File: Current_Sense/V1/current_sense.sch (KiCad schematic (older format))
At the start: 25 parts, among them J201 1935161, U201 LM4040CYM3-4.1-TR, U202 PGA281AIPWR, U203 ADC141S626CIMM/NOPB

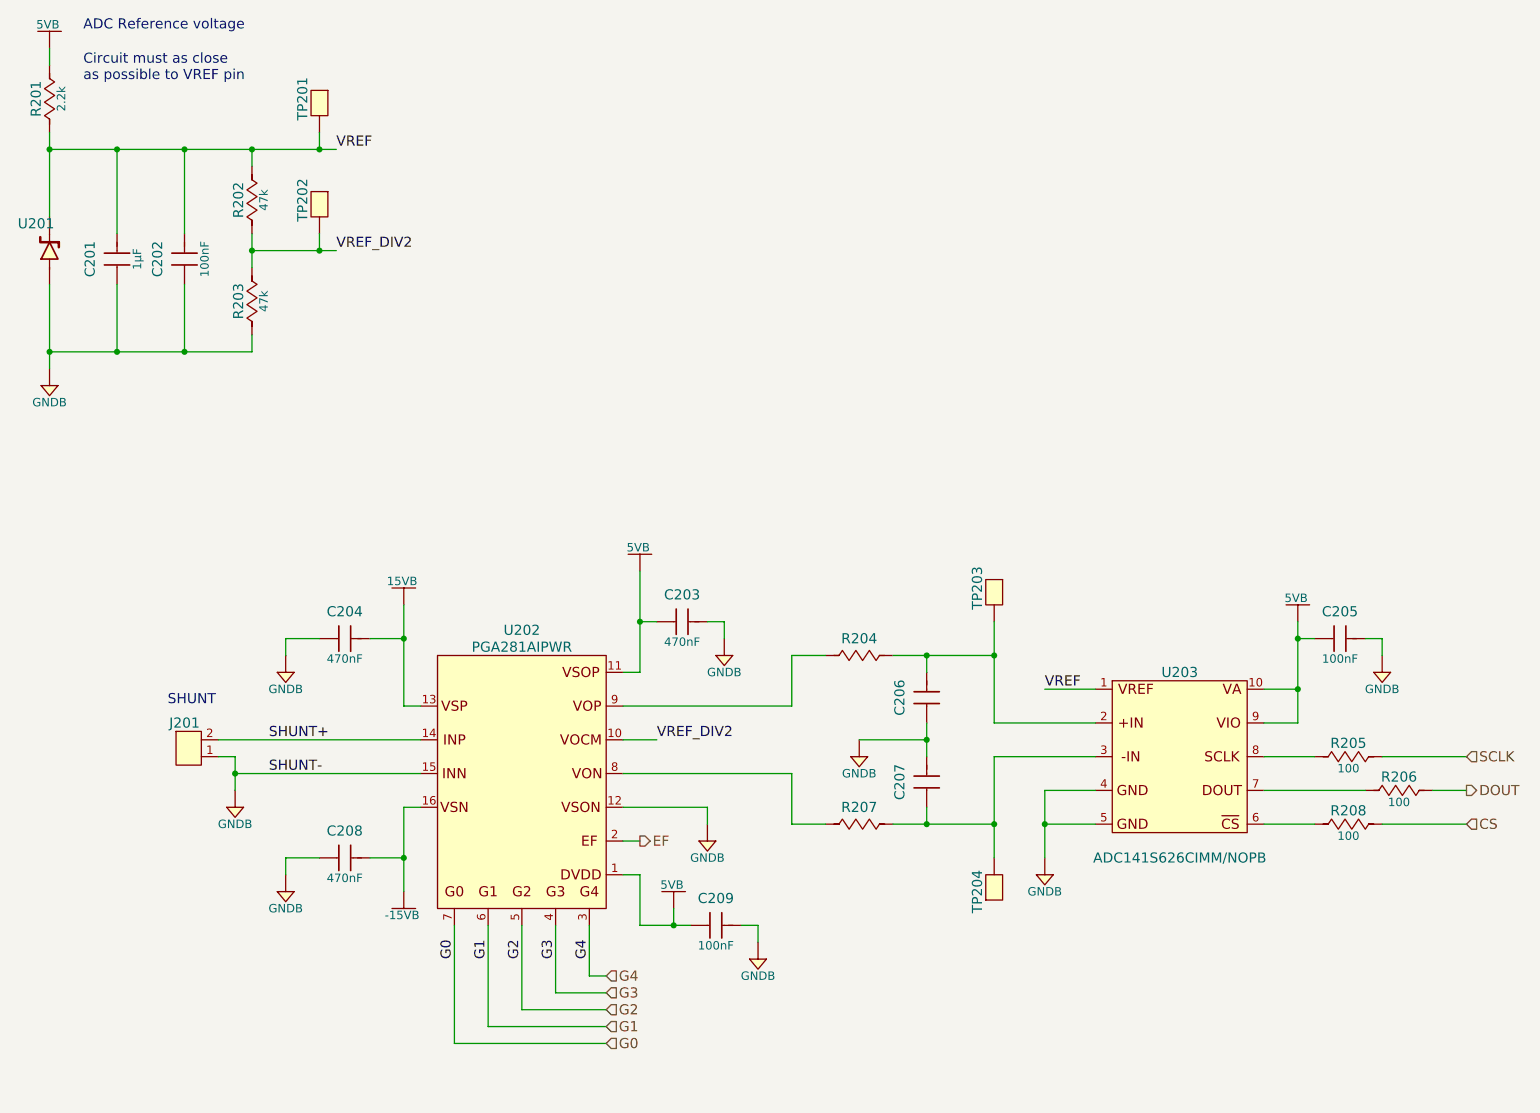
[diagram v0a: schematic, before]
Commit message: add resistor to op amp power
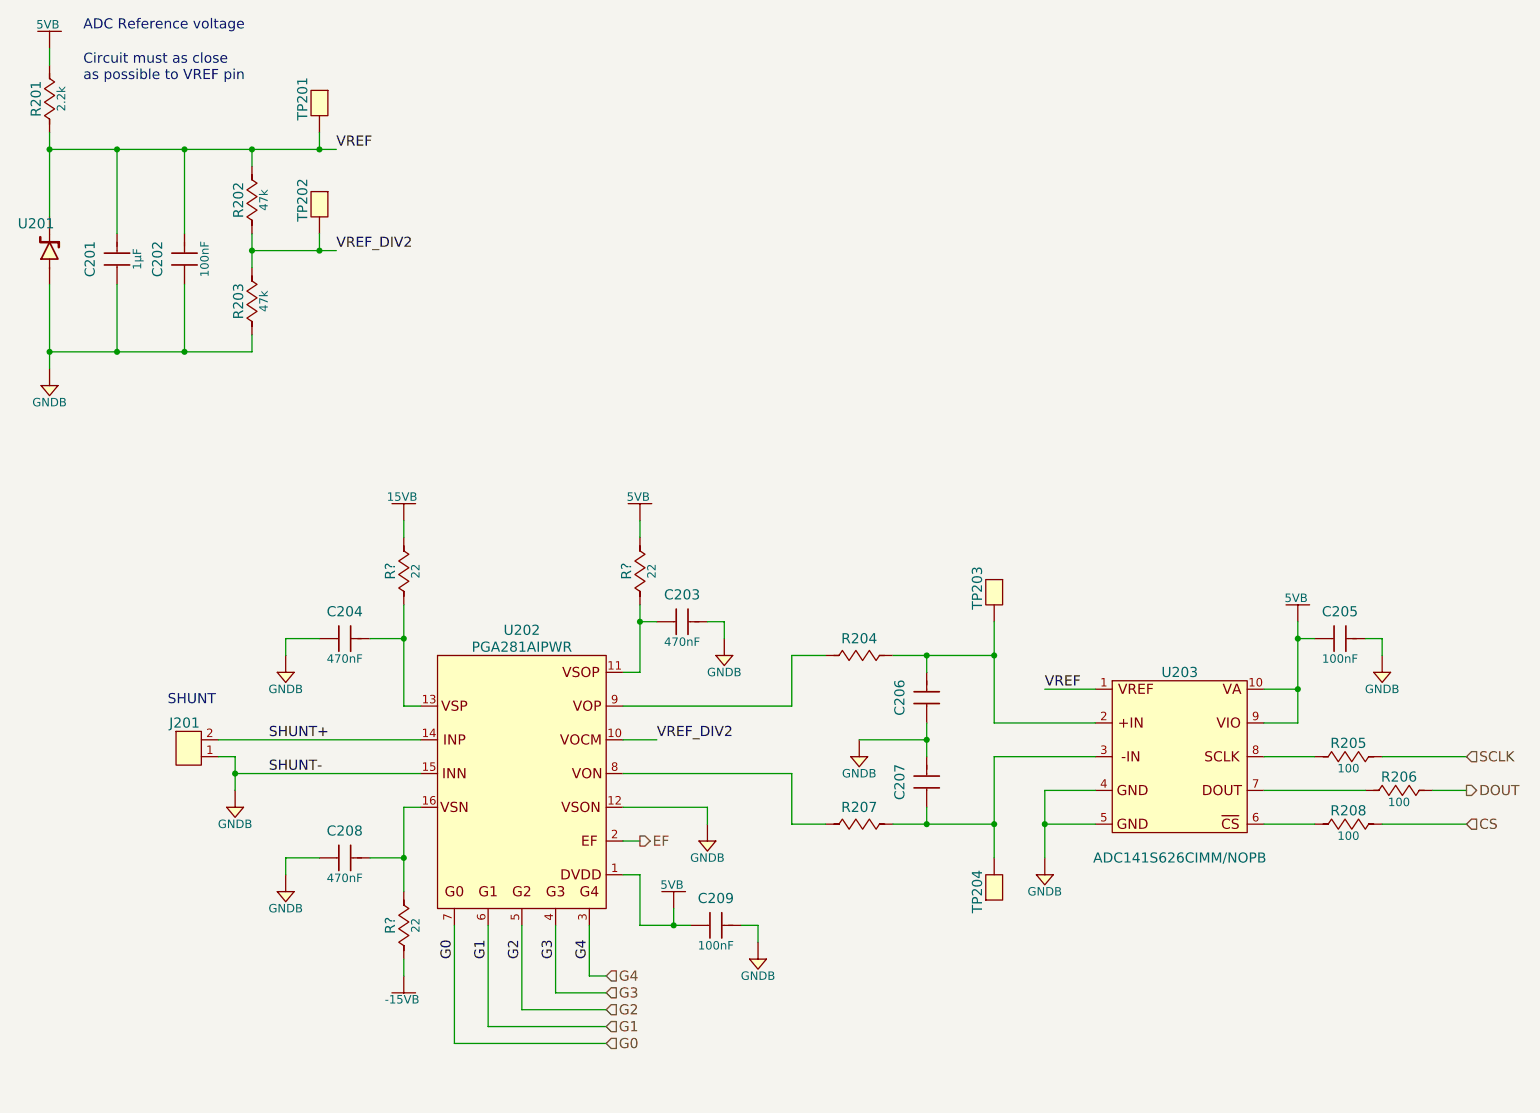
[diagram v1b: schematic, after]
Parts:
- added R? (x3): RC0805JR-0722RL, Resistors:R0805, symbol RC0805JR-0722RL
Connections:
- net -15VB: now also R?.1; no longer C208.2, U202.16 (VSN)
- net 15VB: now also R?.2; no longer C204.2, U202.13 (VSP)
- net 5VB: now also R?.2; no longer C203.1, U202.11 (VSOP)
- new net: C203.1, R?.1, U202.11 (VSOP)
- new net: C204.2, R?.1, U202.13 (VSP)
- new net: C208.2, R?.2, U202.16 (VSN)
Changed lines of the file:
@@
 	1000 800  1000 900
 Wire Wire Line
-	1000 1300 1000 1800
+	1000 1300 1000 1400
+Wire Wire Line
+	1000 1400 1000 1800
 $Comp
 L GNDB #PWR02
@@
 $EndComp
 Wire Wire Line
-	1000 2200 1000 2700
+	1000 2200 1000 2600
+Wire Wire Line
+	1000 2600 1000 2700
 $Comp
 L 885012207098 C202
@@
 $EndComp
 Wire Wire Line
-	1000 1400 2700 1400
+	1000 1400 1400 1400
+Wire Wire Line
+	1400 1400 1800 1400
+Wire Wire Line
+	1800 1400 2200 1400
+Wire Wire Line
+	2200 1400 2600 1400
+Wire Wire Line
+	2600 1400 2700 1400
 Wire Wire Line
 	1400 1400 1400 1900
@@
 	1800 2600 1800 2200
 Wire Wire Line
-	1000 2600 2200 2600
+	1000 2600 1400 2600
+Wire Wire Line
+	1400 2600 1800 2600
+Wire Wire Line
+	1800 2600 2200 2600
 Connection ~ 1000 2600
 Wire Wire Line
@@
 	7200 5200 6900 5200
 Wire Wire Line
-	6900 5200 6900 5600
+	6900 5200 6900 5400
+Wire Wire Line
+	6900 5400 6900 5600
 Wire Wire Line
 	7200 5400 6900 5400
@@
 Connection ~ 2200 1400
 Wire Wire Line
-	2200 1900 2200 2100
-Wire Wire Line
-	2200 2000 2700 2000
+	2200 1900 2200 2000
+Wire Wire Line
+	2200 2000 2200 2100
+Wire Wire Line
+	2200 2000 2600 2000
+Wire Wire Line
+	2600 2000 2700 2000
 Connection ~ 2200 2000
 $Comp
@@
 $EndComp
 Wire Wire Line
-	8400 4200 8400 4800
+	8400 4200 8400 4300
+Wire Wire Line
+	8400 4300 8400 4600
+Wire Wire Line
+	8400 4600 8400 4800
 Wire Wire Line
 	8400 4300 8500 4300
@@
 L 5VB #PWR07
 U 1 1 592E5071
-P 4500 3900
-F 0 "#PWR07" H 4500 3750 50  0001 C CNN
-F 1 "5VB" H 4490 4040 50  0000 C CNN
-F 2 "" H 4500 3900 60  0000 C CNN
-F 3 "" H 4500 3900 60  0000 C CNN
-	1    4500 3900
-	1    0    0    -1
-$EndComp
-Wire Wire Line
-	4500 3900 4500 4500
+P 4500 3600
+F 0 "#PWR07" H 4500 3450 50  0001 C CNN
+F 1 "5VB" H 4490 3740 50  0000 C CNN
+F 2 "" H 4500 3600 60  0000 C CNN
+F 3 "" H 4500 3600 60  0000 C CNN
+	1    4500 3600
+	1    0    0    -1
+$EndComp
+Wire Wire Line
+	4500 4100 4500 4200
+Wire Wire Line
+	4500 4200 4500 4500
 Wire Wire Line
 	4500 4500 4400 4500
@@
 L -15VB #PWR010
 U 1 1 592E5864
-P 3100 5800
-F 0 "#PWR010" H 3100 5520 50  0001 C CNN
-F 1 "-15VB" H 3090 5660 50  0000 C CNN
-F 2 "" H 3100 5800 60  0000 C CNN
-F 3 "" H 3100 5800 60  0000 C CNN
-	1    3100 5800
+P 3100 6300
+F 0 "#PWR010" H 3100 6020 50  0001 C CNN
+F 1 "-15VB" H 3090 6160 50  0000 C CNN
+F 2 "" H 3100 6300 60  0000 C CNN
+F 3 "" H 3100 6300 60  0000 C CNN
+	1    3100 6300
 	1    0    0    -1
 $EndComp
@@
 	3200 5300 3100 5300
 Wire Wire Line
-	3100 5300 3100 5800
+	3100 5300 3100 5600
+Wire Wire Line
+	3100 5600 3100 5800
 Wire Wire Line
 	2900 5600 3100 5600
@@
 L 15VB #PWR012
 U 1 1 592E5ACE
-P 3100 4100
-F 0 "#PWR012" H 3100 3950 50  0001 C CNN
-F 1 "15VB" H 3090 4240 50  0000 C CNN
-F 2 "" H 3100 4100 60  0000 C CNN
-F 3 "" H 3100 4100 60  0000 C CNN
-	1    3100 4100
-	1    0    0    -1
-$EndComp
-Wire Wire Line
-	3100 4100 3100 4700
+P 3100 3600
+F 0 "#PWR012" H 3100 3450 50  0001 C CNN
+F 1 "15VB" H 3090 3740 50  0000 C CNN
+F 2 "" H 3100 3600 60  0000 C CNN
+F 3 "" H 3100 3600 60  0000 C CNN
+	1    3100 3600
+	1    0    0    -1
+$EndComp
+Wire Wire Line
+	3100 4100 3100 4300
+Wire Wire Line
+	3100 4300 3100 4700
 Wire Wire Line
 	3100 4300 2900 4300
@@
 $EndComp
 Wire Wire Line
-	6200 4800 6200 5000
+	6200 4800 6200 4900
+Wire Wire Line
+	6200 4900 6200 5000
 Wire Wire Line
 	5800 4900 6200 4900
 Connection ~ 6200 4900
 Wire Wire Line
-	6000 4400 6600 4400
+	6000 4400 6200 4400
+Wire Wire Line
+	6200 4400 6600 4400
 Wire Wire Line
 	6200 4400 6200 4500
 Wire Wire Line
-	6000 5400 6600 5400
+	6000 5400 6200 5400
+Wire Wire Line
+	6200 5400 6600 5400
 Wire Wire Line
 	6200 5400 6200 5300
@@
 	5400 5400 5600 5400
 Wire Wire Line
-	6600 4200 6600 4800
+	6600 4200 6600 4400
+Wire Wire Line
+	6600 4400 6600 4800
 Connection ~ 6200 4400
 Wire Wire Line
-	6600 5000 6600 5600
+	6600 5000 6600 5400
+Wire Wire Line
+	6600 5400 6600 5600
 Connection ~ 6200 5400
 Wire Wire Line
@@
 	2000 5000 2100 5000
 Wire Wire Line
-	2100 5000 2100 5200
+	2100 5000 2100 5100
+Wire Wire Line
+	2100 5100 2100 5200
 Wire Wire Line
 	2000 4900 3200 4900
@@
 $EndComp
 Wire Wire Line
-	4500 6000 4800 6000
+	4500 6000 4700 6000
+Wire Wire Line
+	4700 6000 4800 6000
 $Comp
 L GNDB #PWR015
@@
 Text Label 2700 2000 0    60   ~ 0
 VREF_DIV2
+$Comp
+L RC0805JR-0722RL R?
+U 1 1 5951E4F5
+P 3100 3900
+F 0 "R?" H 3100 3980 60  0000 C CNN
+F 1 "RC0805JR-0722RL" H 3100 3600 50  0001 C CNN
+F 2 "Resistors:R0805" H 3100 3000 30  0001 C CNN
+F 3 "http://www.yageo.com/documents/recent/PYu-RC_Group_51_RoHS_L_7.pdf" H 3100 2950 30  0001 C CNN
+F 4 "Digikey" H 3100 3500 60  0001 C CNN "Supplier"
+F 5 "311-22ARCT-ND" H 3100 3400 60  0001 C CNN "Supplier Part Number"
+F 6 "Yageo" H 3100 3300 60  0001 C CNN "Manufacturer"
+F 7 "RC0805JR-0722RL" H 3100 3200 60  0001 C CNN "Manufacturer Part Number"
+F 8 "RES SMD 22 OHM 5% 1/8W 0805" H 3100 3100 60  0001 C CNN "Description"
+F 9 "22" H 3100 3830 50  0000 C CNN "Resistance (Ohms)"
+F 10 "±5%" H 3510 3820 50  0001 C CNN "Tolerance (%)"
+F 11 "1/8W" H 3100 3760 50  0001 C CNN "Puissance (Watts)"
+	1    3100 3900
+	0    -1   -1   0
+$EndComp
+Wire Wire Line
+	3100 3600 3100 3700
+$Comp
+L RC0805JR-0722RL R?
+U 1 1 5951F097
+P 3100 6000
+F 0 "R?" H 3100 6080 60  0000 C CNN
+F 1 "RC0805JR-0722RL" H 3100 5700 50  0001 C CNN
+F 2 "Resistors:R0805" H 3100 5100 30  0001 C CNN
+F 3 "http://www.yageo.com/documents/recent/PYu-RC_Group_51_RoHS_L_7.pdf" H 3100 5050 30  0001 C CNN
+F 4 "Digikey" H 3100 5600 60  0001 C CNN "Supplier"
+F 5 "311-22ARCT-ND" H 3100 5500 60  0001 C CNN "Supplier Part Number"
+F 6 "Yageo" H 3100 5400 60  0001 C CNN "Manufacturer"
+F 7 "RC0805JR-0722RL" H 3100 5300 60  0001 C CNN "Manufacturer Part Number"
+F 8 "RES SMD 22 OHM 5% 1/8W 0805" H 3100 5200 60  0001 C CNN "Description"
+F 9 "22" H 3100 5930 50  0000 C CNN "Resistance (Ohms)"
+F 10 "±5%" H 3510 5920 50  0001 C CNN "Tolerance (%)"
+F 11 "1/8W" H 3100 5860 50  0001 C CNN "Puissance (Watts)"
+	1    3100 6000
+	0    -1   -1   0
+$EndComp
+Wire Wire Line
+	3100 6200 3100 6300
+$Comp
+L RC0805JR-0722RL R?
+U 1 1 5951FC2F
+P 4500 3900
+F 0 "R?" H 4500 3980 60  0000 C CNN
+F 1 "RC0805JR-0722RL" H 4500 3600 50  0001 C CNN
+F 2 "Resistors:R0805" H 4500 3000 30  0001 C CNN
+F 3 "http://www.yageo.com/documents/recent/PYu-RC_Group_51_RoHS_L_7.pdf" H 4500 2950 30  0001 C CNN
+F 4 "Digikey" H 4500 3500 60  0001 C CNN "Supplier"
+F 5 "311-22ARCT-ND" H 4500 3400 60  0001 C CNN "Supplier Part Number"
+F 6 "Yageo" H 4500 3300 60  0001 C CNN "Manufacturer"
+F 7 "RC0805JR-0722RL" H 4500 3200 60  0001 C CNN "Manufacturer Part Number"
+F 8 "RES SMD 22 OHM 5% 1/8W 0805" H 4500 3100 60  0001 C CNN "Description"
+F 9 "22" H 4500 3830 50  0000 C CNN "Resistance (Ohms)"
+F 10 "±5%" H 4910 3820 50  0001 C CNN "Tolerance (%)"
+F 11 "1/8W" H 4500 3760 50  0001 C CNN "Puissance (Watts)"
+	1    4500 3900
+	0    -1   -1   0
+$EndComp
+Wire Wire Line
+	4500 3600 4500 3700
 $EndSCHEMATC

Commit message: add comment
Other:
- note added: "Mettre thermistance"
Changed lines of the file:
@@
 	1000 800  1000 900
 Wire Wire Line
-	1000 1300 1000 1400
-Wire Wire Line
-	1000 1400 1000 1800
+	1000 1300 1000 1800
 $Comp
 L GNDB #PWR02
@@
 $EndComp
 Wire Wire Line
-	1000 2200 1000 2600
-Wire Wire Line
-	1000 2600 1000 2700
+	1000 2200 1000 2700
 $Comp
 L 885012207098 C202
@@
 $EndComp
 Wire Wire Line
-	1000 1400 1400 1400
-Wire Wire Line
-	1400 1400 1800 1400
-Wire Wire Line
-	1800 1400 2200 1400
-Wire Wire Line
-	2200 1400 2600 1400
-Wire Wire Line
-	2600 1400 2700 1400
+	1000 1400 2700 1400
 Wire Wire Line
 	1400 1400 1400 1900
@@
 	1800 2600 1800 2200
 Wire Wire Line
-	1000 2600 1400 2600
-Wire Wire Line
-	1400 2600 1800 2600
-Wire Wire Line
-	1800 2600 2200 2600
+	1000 2600 2200 2600
 Connection ~ 1000 2600
 Wire Wire Line
@@
 	7200 5200 6900 5200
 Wire Wire Line
-	6900 5200 6900 5400
-Wire Wire Line
-	6900 5400 6900 5600
+	6900 5200 6900 5600
 Wire Wire Line
 	7200 5400 6900 5400
@@
 Connection ~ 2200 1400
 Wire Wire Line
-	2200 1900 2200 2000
-Wire Wire Line
-	2200 2000 2200 2100
-Wire Wire Line
-	2200 2000 2600 2000
-Wire Wire Line
-	2600 2000 2700 2000
+	2200 1900 2200 2100
+Wire Wire Line
+	2200 2000 2700 2000
 Connection ~ 2200 2000
 $Comp
@@
 $EndComp
 Wire Wire Line
-	8400 4200 8400 4300
-Wire Wire Line
-	8400 4300 8400 4600
-Wire Wire Line
-	8400 4600 8400 4800
+	8400 4200 8400 4800
 Wire Wire Line
 	8400 4300 8500 4300
@@
 $EndComp
 Wire Wire Line
-	4500 4100 4500 4200
-Wire Wire Line
-	4500 4200 4500 4500
+	4500 4100 4500 4500
 Wire Wire Line
 	4500 4500 4400 4500
@@
 	3200 5300 3100 5300
 Wire Wire Line
-	3100 5300 3100 5600
-Wire Wire Line
-	3100 5600 3100 5800
+	3100 5300 3100 5800
 Wire Wire Line
 	2900 5600 3100 5600
@@
 $EndComp
 Wire Wire Line
-	3100 4100 3100 4300
-Wire Wire Line
-	3100 4300 3100 4700
+	3100 4100 3100 4700
 Wire Wire Line
 	3100 4300 2900 4300
@@
 $EndComp
 Wire Wire Line
-	6200 4800 6200 4900
-Wire Wire Line
-	6200 4900 6200 5000
+	6200 4800 6200 5000
 Wire Wire Line
 	5800 4900 6200 4900
 Connection ~ 6200 4900
 Wire Wire Line
-	6000 4400 6200 4400
-Wire Wire Line
-	6200 4400 6600 4400
+	6000 4400 6600 4400
 Wire Wire Line
 	6200 4400 6200 4500
 Wire Wire Line
-	6000 5400 6200 5400
-Wire Wire Line
-	6200 5400 6600 5400
+	6000 5400 6600 5400
 Wire Wire Line
 	6200 5400 6200 5300
@@
 	5400 5400 5600 5400
 Wire Wire Line
-	6600 4200 6600 4400
-Wire Wire Line
-	6600 4400 6600 4800
+	6600 4200 6600 4800
 Connection ~ 6200 4400
 Wire Wire Line
-	6600 5000 6600 5400
-Wire Wire Line
-	6600 5400 6600 5600
+	6600 5000 6600 5600
 Connection ~ 6200 5400
 Wire Wire Line
@@
 	2000 5000 2100 5000
 Wire Wire Line
-	2100 5000 2100 5100
-Wire Wire Line
-	2100 5100 2100 5200
+	2100 5000 2100 5200
 Wire Wire Line
 	2000 4900 3200 4900
@@
 $EndComp
 Wire Wire Line
-	4500 6000 4700 6000
-Wire Wire Line
-	4700 6000 4800 6000
+	4500 6000 4800 6000
 $Comp
 L GNDB #PWR015
@@
 Wire Wire Line
 	4500 3600 4500 3700
+Text Notes 1300 4000 0    60   ~ 0
+Mettre thermistance
 $EndSCHEMATC
